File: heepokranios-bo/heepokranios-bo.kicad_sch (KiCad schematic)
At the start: 124 parts, among them J1 Conn_02x02_Odd_Even, J11 PGA_13x13, J12 Conn_01x02, J13 Conn_01x02, J14 Conn_02x03_Odd_Even, J15 Conn_02x08_Odd_Even, J16 Conn_02x03_Odd_Even, J17 Conn_02x03_Odd_Even, J2 Conn_02x02_Odd_Even, J3 Conn_02x03_Odd_Even, J4 Conn_02x03_Odd_Even, J5 Conn_02x03_Odd_Even, J6 Conn_02x04_Odd_Even, J8 Conn_02x03_Odd_Even, J9 Conn_02x02_Odd_Even, SW1 SW_Push

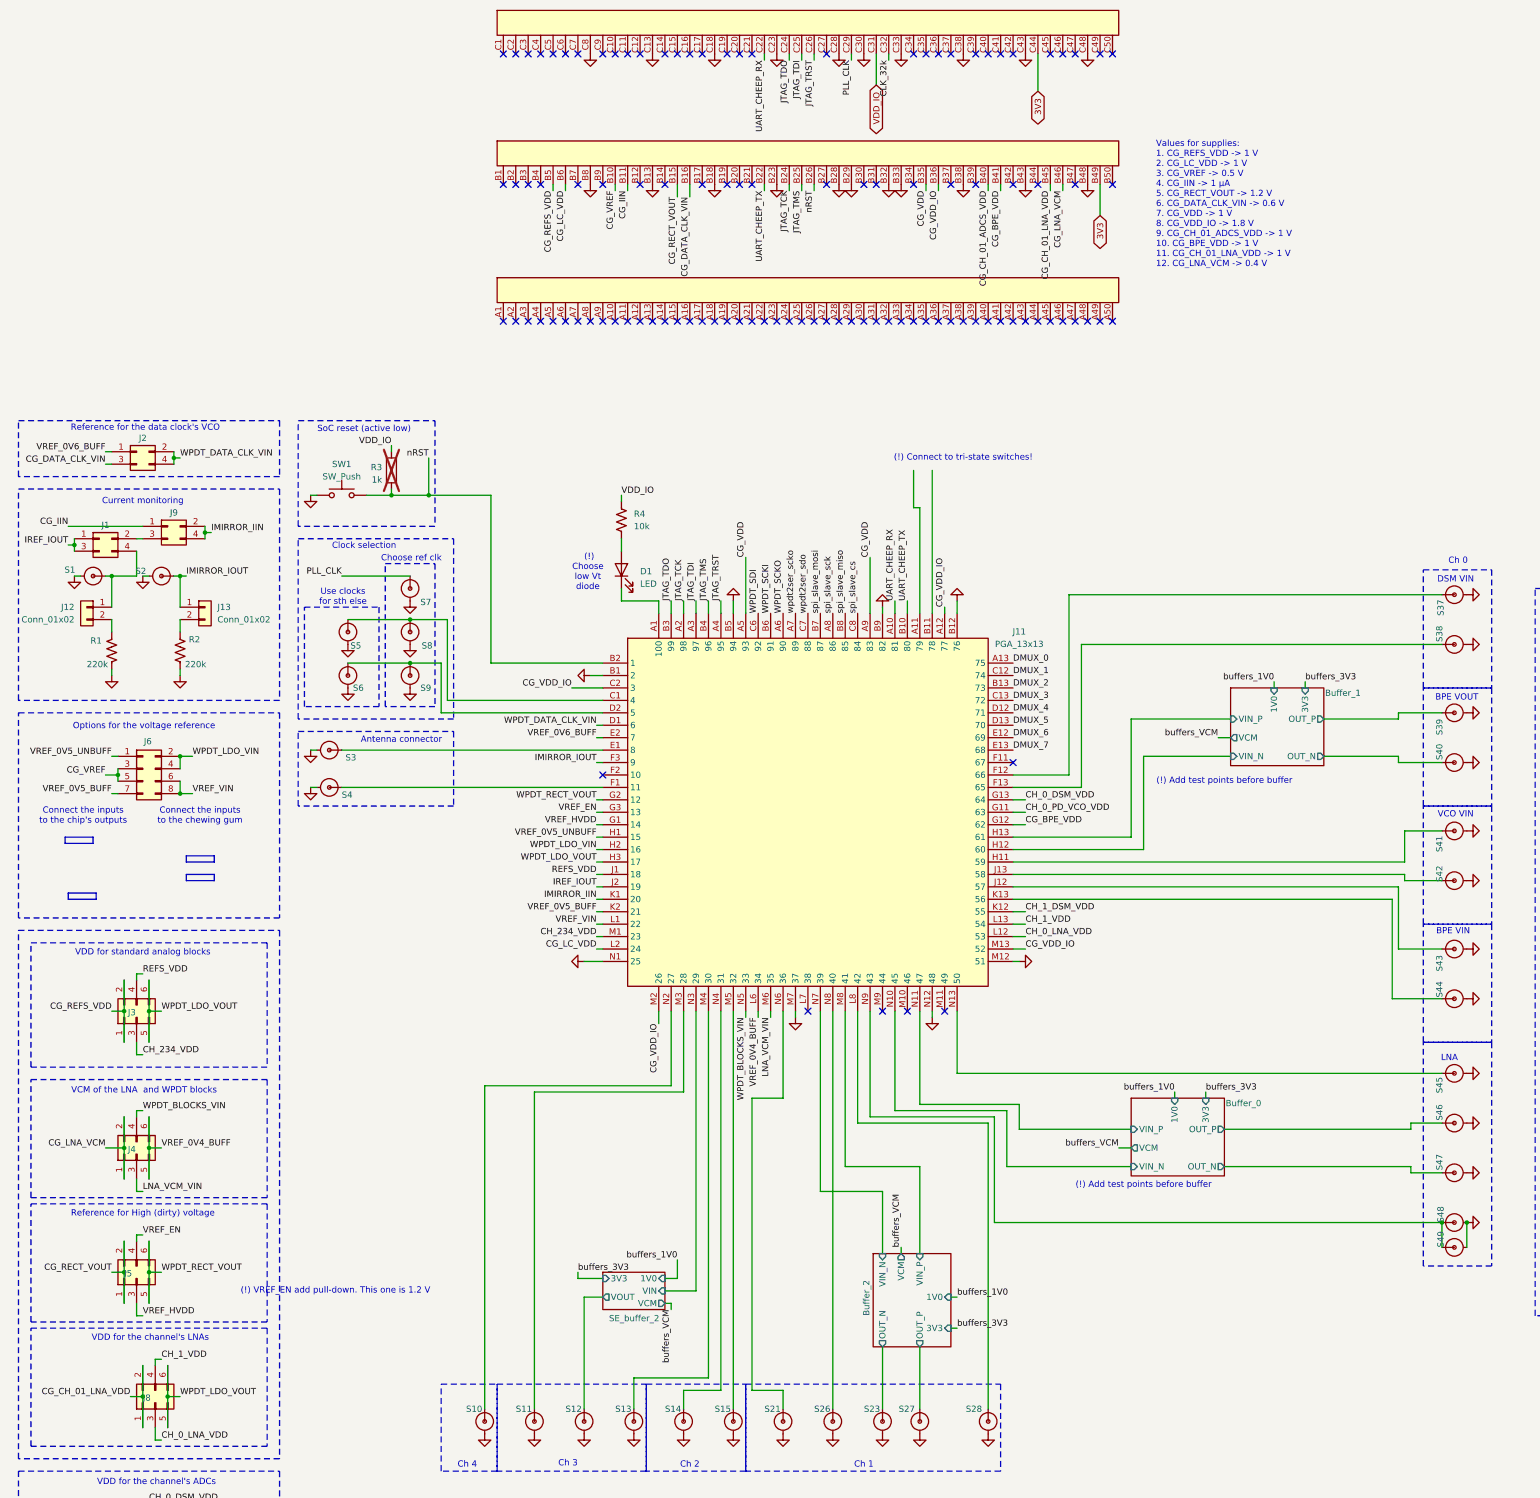
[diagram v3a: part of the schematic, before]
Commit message: Completed layout of the breakout board
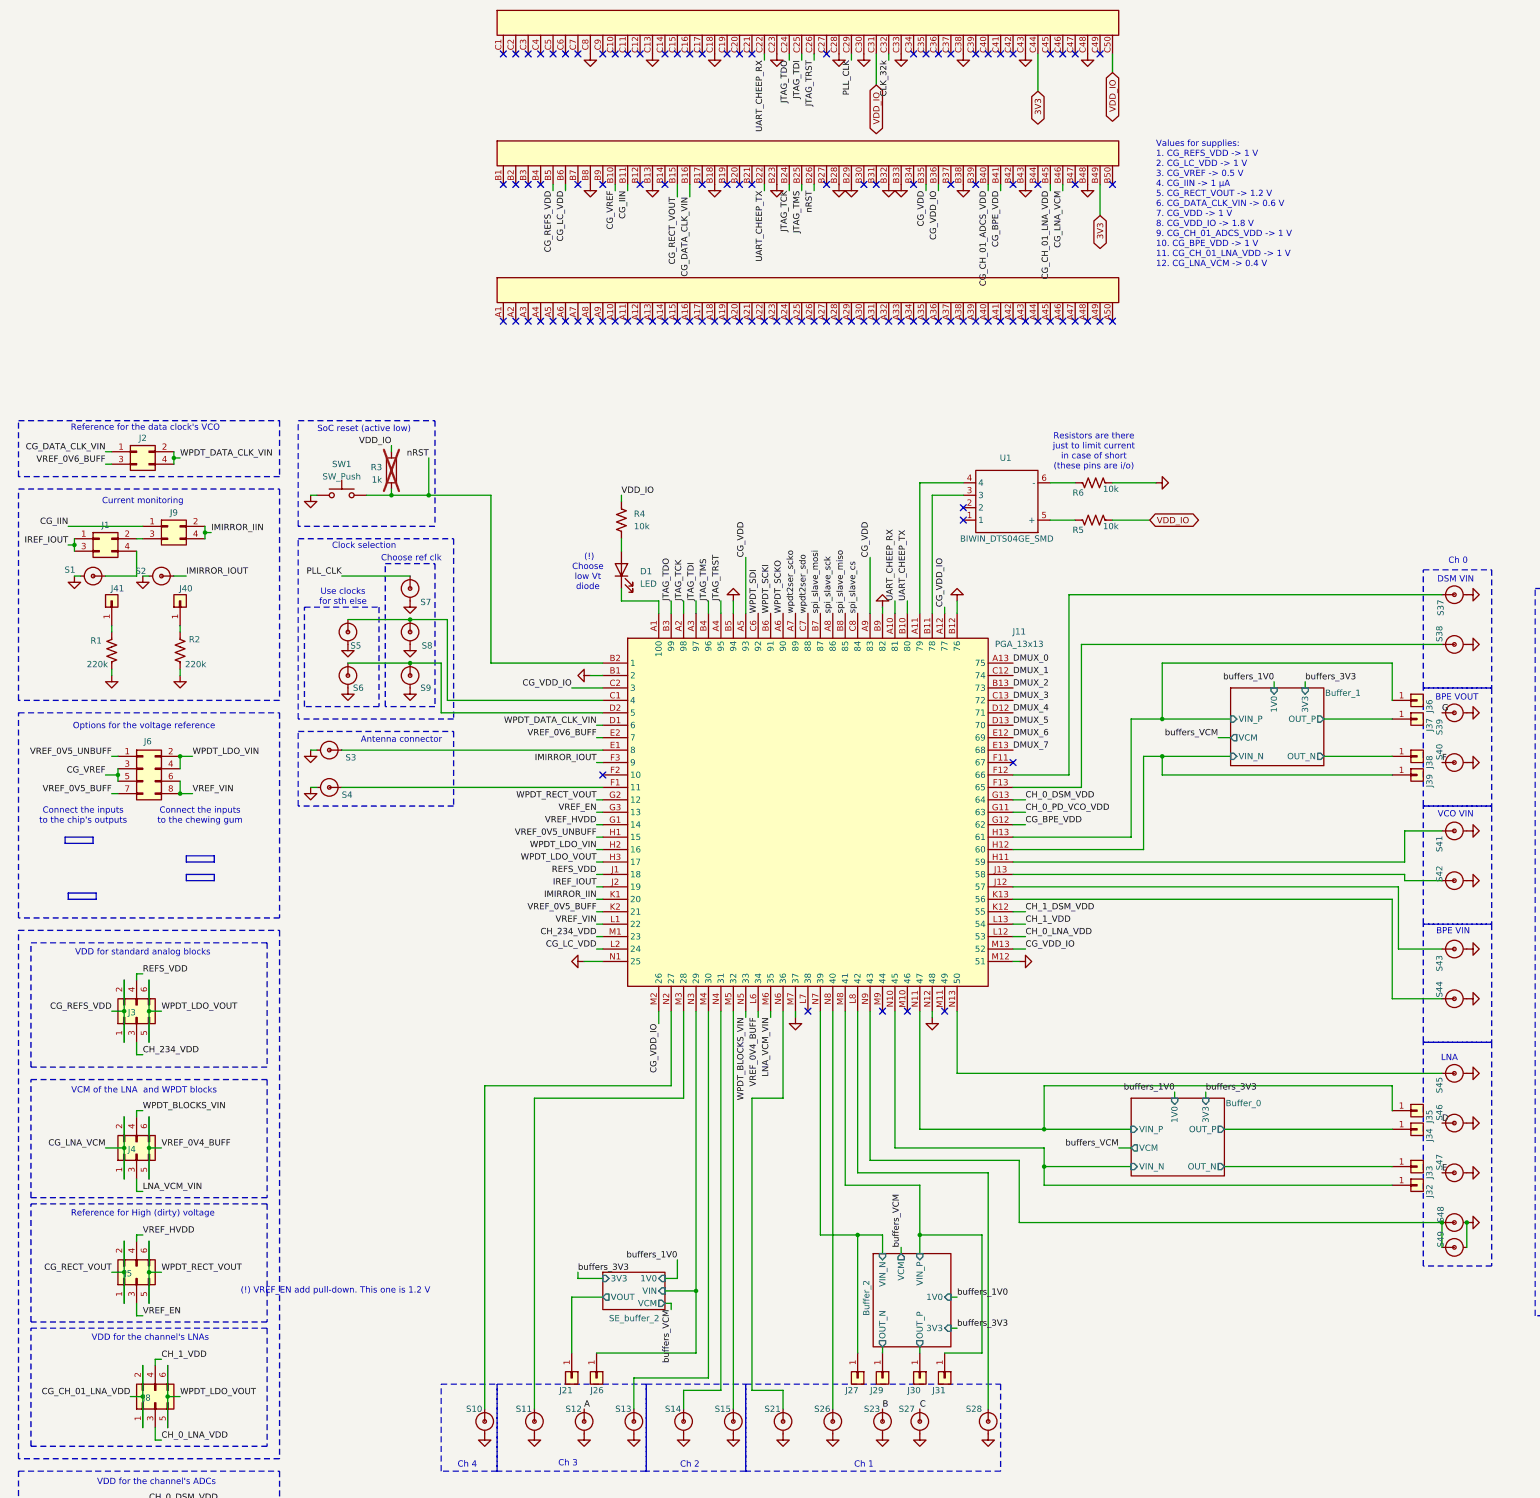
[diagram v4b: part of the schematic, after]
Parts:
- removed J11: PGA_13x13, PGA13x13, symbol PGA_socket:PGA_13x13
- removed J12, J13: Conn_01x02, Connector_PinHeader_2.54mm:PinHeader_1x02_P2.54mm_Vertical, symbol Connector_Generic:Conn_01x02
- added J11: PGA_13x13, heepokranios-bo-library:PGA_13x13, symbol PGA_Socket:PGA_13x13
- added J21, J26, J27, J29, J30, J31, J32, J33, J34, J35, J36, J37, J38, J39, J40, J41: Conn_01x02, Connector_PinHeader_2.54mm:PinHeader_1x01_P2.54mm_Vertical, symbol Connector_Generic:Conn_01x01
- added R5, R6: 10k, Resistor_SMD:R_0603_1608Metric, symbol Device:R_US
- added U1: BIWIN_DTS04GE_SMD, heepokranios-bo-library:BIWIN_DTS04GE_SMD, symbol cheeps-tb:SPDT-4bit-tri-state
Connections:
- net Buffer_0/OUT_N: now also J33.1 (Pin_1); no longer S47.1
- net Buffer_0/OUT_P: now also J34.1 (Pin_1); no longer S46.1
- net Buffer_0/VIN_N: now also J11.N10 (45), J32.1 (Pin_1)
- net Buffer_0/VIN_P: now also J11.N11 (47), J35.1 (Pin_1)
- net Buffer_1/OUT_N: now also J38.1 (Pin_1); no longer S40.1
- net Buffer_1/OUT_P: now also J37.1 (Pin_1); no longer S39.1
- net Buffer_1/VIN_N: now also J11.H12 (60), J39.1 (Pin_1)
- net Buffer_1/VIN_P: now also J11.H13 (61), J36.1 (Pin_1)
- net Buffer_2/OUT_N: now also J29.1 (Pin_1); no longer S23.1
- net Buffer_2/OUT_P: now also J30.1 (Pin_1); no longer S27.1
- net Buffer_2/VIN_N: now also J11.N7 (39), J27.1 (Pin_1)
- net Buffer_2/VIN_P: now also J11.M8 (41), J31.1 (Pin_1)
- net CG_BPE_VDD: now also J11.G12 (62)
- net CG_DATA_CLK_VIN: now also J2.1 (Pin_1); no longer J2.3 (Pin_3)
- net CG_LC_VDD: now also J11.L2 (24)
- net CG_VDD: now also J11.A5 (93), J11.A9 (83)
- net CG_VDD_IO: now also J11.A12 (77), J11.C2 (3), J11.M13 (52), J11.M2 (26)
- net CH_0_DSM_VDD: now also J11.G13 (64)
- net CH_0_LNA_VDD: now also J11.L12 (53)
- net CH_0_PD_VCO_VDD: now also J11.G11 (63)
- net CH_1_DSM_VDD: now also J11.K12 (55)
- net CH_1_VDD: now also J11.L13 (54)
- net CH_234_VDD: now also J11.M1 (23)
- net DMUX_0: now also J11.A13 (75)
- net DMUX_1: now also J11.C12 (74)
- net DMUX_2: now also J11.B13 (73)
- net DMUX_3: now also J11.C13 (72)
- net DMUX_4: now also J11.D12 (71)
- net DMUX_5: now also J11.D13 (70)
- net DMUX_6: now also J11.E12 (69)
- net DMUX_7: now also J11.E13 (68)
- net GND: now also J11.B1 (2), J11.B12 (76), J11.B5 (94), J11.B9 (82), J11.M12 (51), J11.M7 (37), J11.N1 (25), J11.N12 (48), R6.2
- net IMIRROR_IIN: now also J11.K1 (20)
- net IMIRROR_IOUT: now also J11.F3 (9)
- net IREF_IOUT: now also J11.J2 (19)
- net JTAG_TCK: now also J11.A2 (98)
- net JTAG_TDI: now also J11.A3 (97)
- net JTAG_TDO: now also J11.B3 (99)
- net JTAG_TMS: now also J11.B4 (96)
- net JTAG_TRST: now also J11.A4 (95)
- net LNA_VCM_VIN: now also J11.M6 (35)
- net REFS_VDD: now also J11.J1 (18)
- net SE_buffer_2/VIN: now also J11.N3 (29), J26.1 (Pin_1)
- net SE_buffer_2/VOUT: now also J21.1 (Pin_1); no longer S12.1
- net UART_CHEEP_RX: now also J11.A10 (81)
- net UART_CHEEP_TX: now also J11.B10 (80)
- net VDD_IO: now also J10.C50, R5.2
- net VREF_0V4_BUFF: now also J11.L6 (34)
- net VREF_0V5_BUFF: now also J11.K2 (21)
- net VREF_0V5_UNBUFF: now also J11.H1 (15)
- net VREF_0V6_BUFF: now also J2.3 (Pin_3), J11.E2 (7); no longer J2.1 (Pin_1)
- net VREF_EN: now also J5.3 (Pin_3), J11.G3 (13); no longer J5.4 (Pin_4)
- net VREF_HVDD: now also J5.4 (Pin_4), J11.G1 (14); no longer J5.3 (Pin_3)
- net VREF_VIN: now also J11.L1 (22)
- net WPDT_BLOCKS_VIN: now also J11.N5 (33)
- net WPDT_DATA_CLK_VIN: now also J11.D1 (6)
- net WPDT_LDO_VIN: now also J11.H2 (16)
- net WPDT_LDO_VOUT: now also J11.H3 (17)
- net WPDT_RECT_VOUT: now also J11.G2 (12)
- net WPDT_SCKI: now also J11.B6 (91)
- net WPDT_SCKO: now also J11.A6 (90)
- net WPDT_SDI: now also J11.C6 (92)
- net nRST: now also J11.B2 (1)
- net spi_slave_cs: now also J11.C8 (84)
- net spi_slave_miso: now also J11.B8 (85)
- net spi_slave_mosi: now also J11.B7 (87)
- net spi_slave_sck: now also J11.A8 (86)
- net wpdt2ser_scko: now also J11.A7 (89)
- net wpdt2ser_sdo: now also J11.C7 (88)
- net at S43.1: now also J11.J12 (57)
- net at R2.1: now also J40.1 (Pin_1)
- net at D1.1 (K): now also J11.A1 (100)
- net at S13.1: now also J11.M4 (30)
- net at S5.1, S8.1: now also J11.C1 (4)
- net at S28.1: now also J11.L8 (42)
- net at S4.1: now also J11.F1 (11)
- net at S6.1, S9.1: now also J11.D2 (5)
- net at S37.1: now also J11.F12 (66)
- net at S45.1: now also J11.N13 (50)
- net at S42.1: now also J11.J13 (58)
- net at S41.1: now also J11.H11 (59)
- net at R1.1: now also J41.1 (Pin_1)
- net at S3.1: now also J11.E1 (8)
- net at S38.1: now also J11.F13 (65)
- net at S44.1: now also J11.K13 (56)
- net at S11.1: now also J11.M3 (28)
- net at S15.1: now also J11.M5 (32)
- net at S10.1: now also J11.N2 (27)
- net at S14.1: now also J11.N4 (31)
- net at S21.1: now also J11.N6 (36)
- net at S26.1: now also J11.N8 (40)
- net at S48.1, S49.1: now also J11.N9 (43)
- new net: J11.A11 (79), U1.4
- new net: J11.B11 (78), U1.3
- new net: R6.1, U1.6 (-)
- new net: R5.1, U1.5 (+)
- new net A: S12.1
- new net B: S23.1
- new net C: S27.1
- new net D: S46.1
- new net E: S47.1
- new net F: S40.1
- new net G: S39.1
- no-connect marks 111 -> 112
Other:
- note added: "Resistors are there just to limit current in case of short (these pins are i/o)"
- note removed: "(!) Add test points before buffer"
- note removed: "(!) Connect to tri-state switches!"

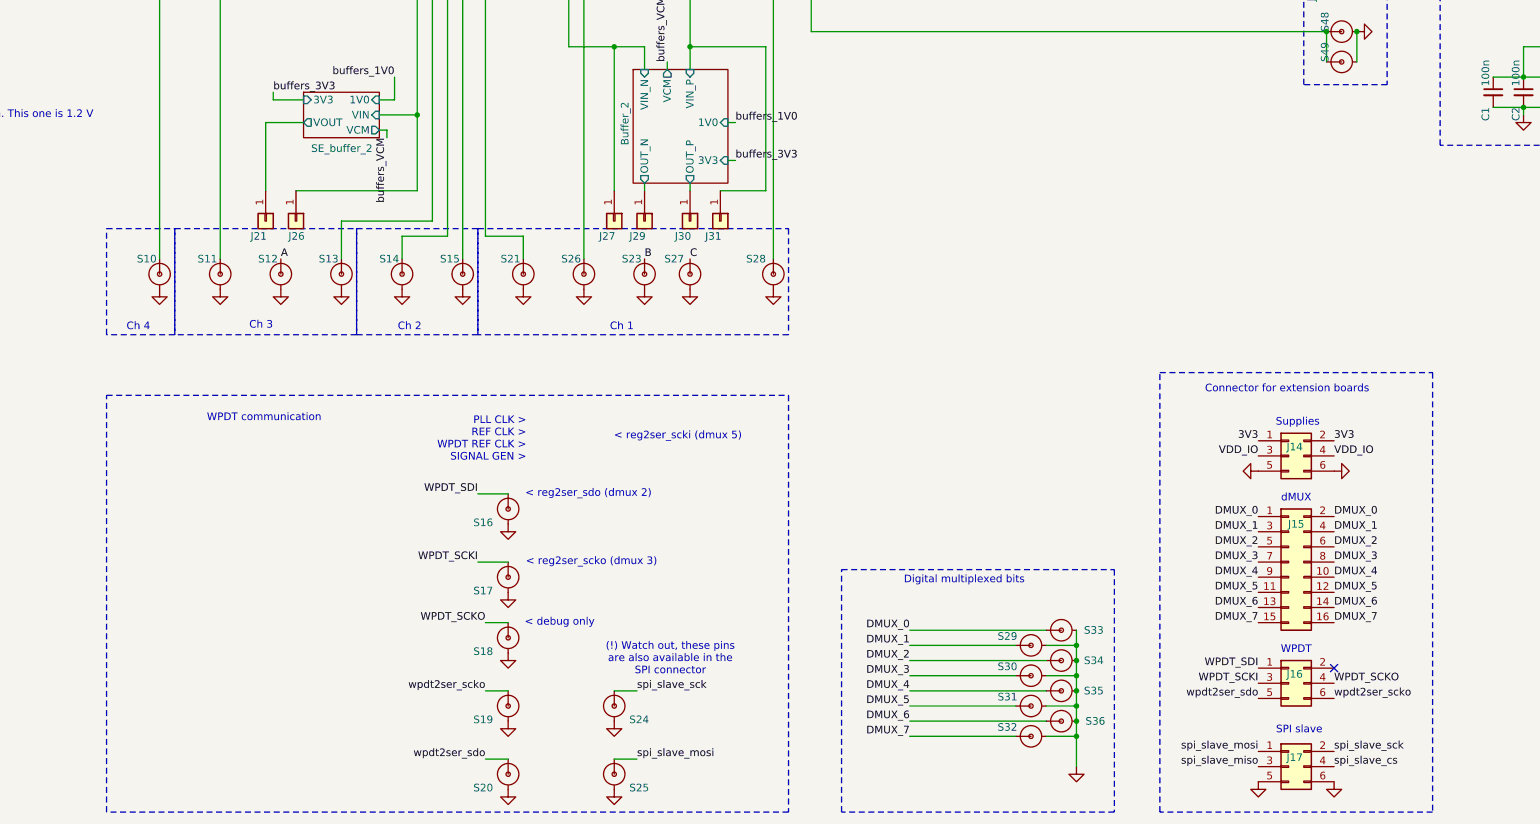
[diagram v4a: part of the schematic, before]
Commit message: Added logos to breakout
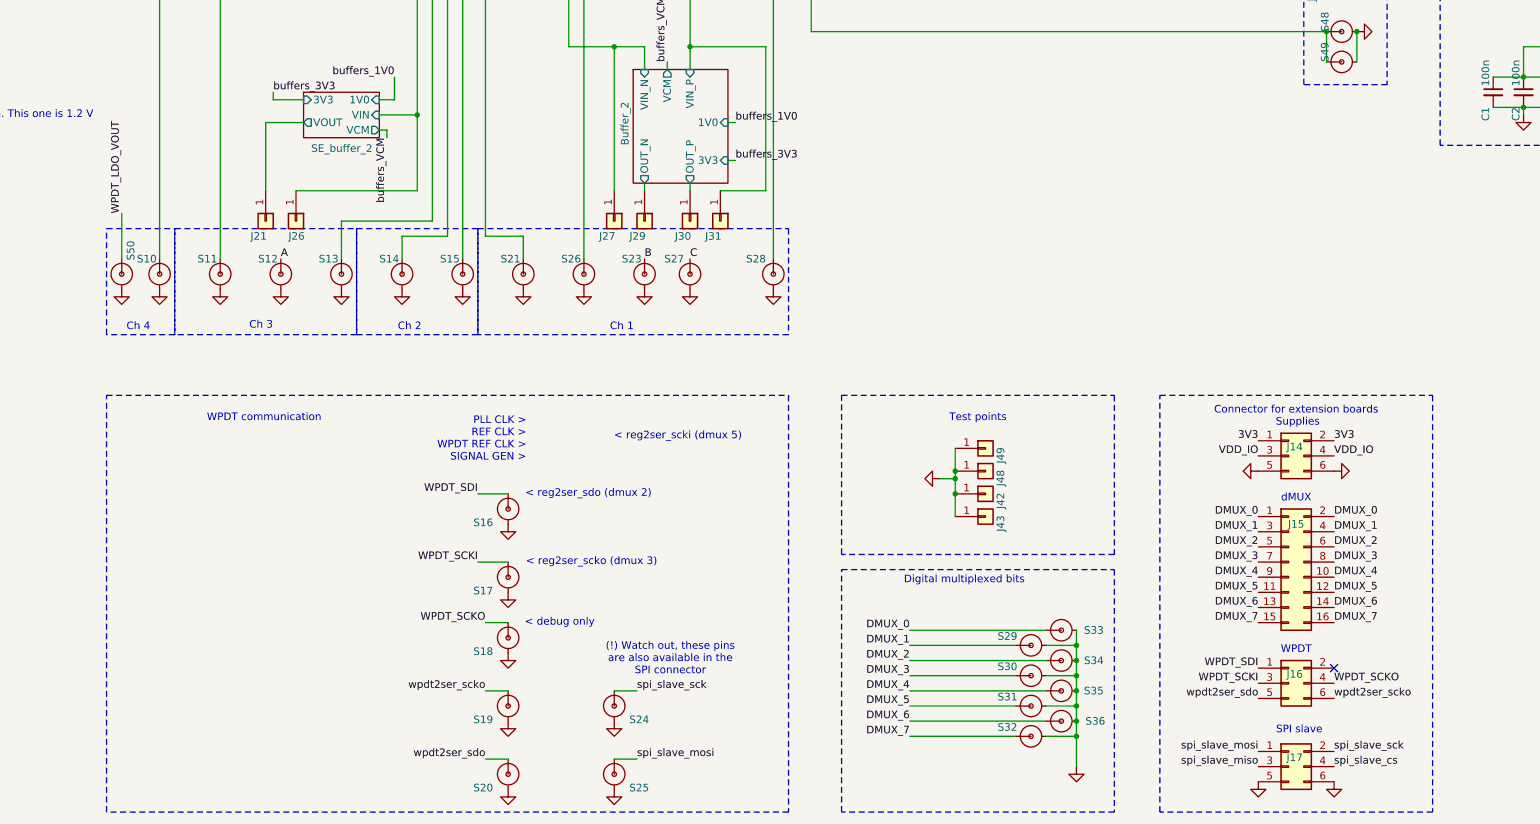
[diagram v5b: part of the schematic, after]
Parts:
- added J42, J43, J48, J49: Conn_01x02, Connector_PinHeader_2.54mm:PinHeader_1x01_P2.54mm_Vertical, symbol Connector_Generic:Conn_01x01
- added S50: SMA connector, heepokranios-bo-library:SMA_w_tp, symbol heepokranios-bo-library:SMA_w_tp
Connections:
- net GND: now also J42.1 (Pin_1), J43.1 (Pin_1), J48.1 (Pin_1), J49.1 (Pin_1), S50.2
- net WPDT_LDO_VOUT: now also S50.1
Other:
- note added: "Test points"
